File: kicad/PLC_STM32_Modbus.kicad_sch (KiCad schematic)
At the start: 0 parts

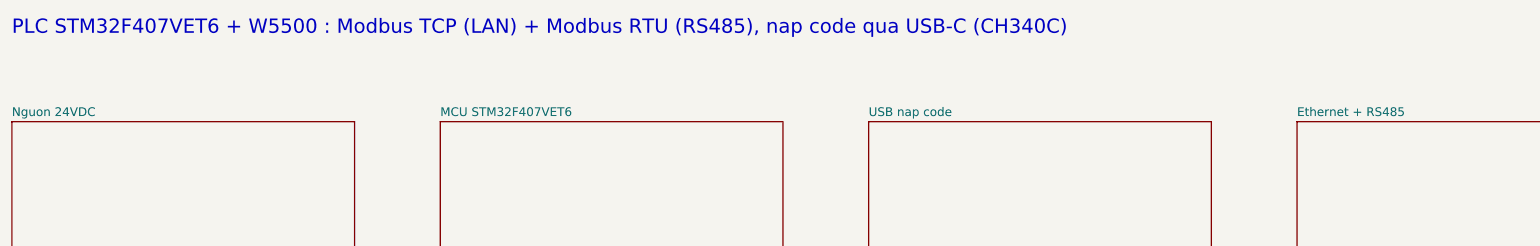
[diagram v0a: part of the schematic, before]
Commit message: - bỏ các mạch 0-10v, RS485 RTU
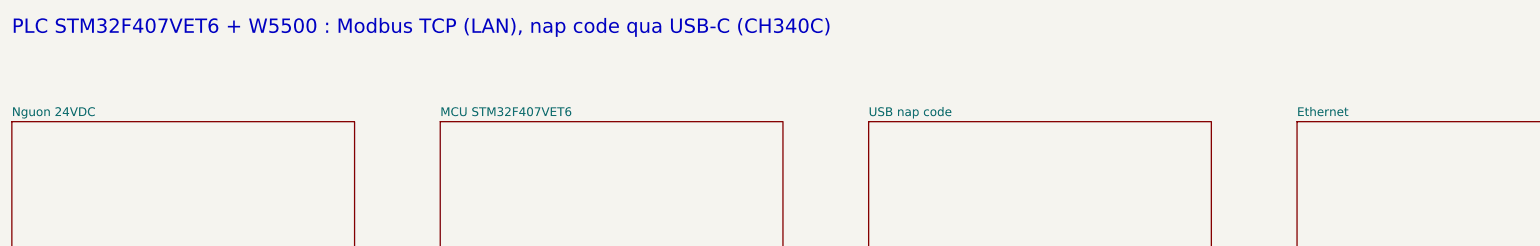
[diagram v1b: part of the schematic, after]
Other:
- removed sheet Ethernet + RS485
- added sheet Ethernet (comm.kicad_sch)
- note added: "PLC STM32F407VET6 + W5500 : Modbus TCP (LAN), nap code qua USB-C (CH340C)"
- note removed: "PLC STM32F407VET6 + W5500 : Modbus TCP (LAN) + Modbus RTU (RS485), nap code qua USB-C (CH340C)"
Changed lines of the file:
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@@
 (kicad_sch
-	(version 20250610)
+	(version 20260306)
 	(generator "eeschema")
 	(generator_version "10.0")
@@
 		(comment 1 "Sheet: Root")
 	)
-	(text "PLC STM32F407VET6 + W5500 : Modbus TCP (LAN) + Modbus RTU (RS485), nap code qua USB-C (CH340C)"
+	(text "PLC STM32F407VET6 + W5500 : Modbus TCP (LAN), nap code qua USB-C (CH340C)"
 		(exclude_from_sim no)
 		(at 30 25 0)
@@
 	)
 	(sheet
+		(at 180 40)
+		(size 60 25)
+		(exclude_from_sim no)
+		(in_bom yes)
+		(on_board yes)
+		(dnp no)
+		(stroke
+			(width 0.1524)
+			(type solid)
+		)
+		(fill
+			(color 0 0 0 0)
+		)
+		(property "Sheetname" "USB nap code"
+			(at 180 39.2 0)
+			(show_name no)
+			(do_not_autoplace no)
+			(effects
+				(font
+					(size 1.524 1.524)
+				)
+				(justify left bottom)
+			)
+		)
+		(property "Sheetfile" "usb.kicad_sch"
+			(at 180 65.6 0)
+			(show_name no)
+			(do_not_autoplace no)
+			(effects
+				(font
+					(size 1.27 1.27)
+				)
+				(justify left top)
+			)
+		)
+		(instances
+			(project "PLC_STM32_Modbus"
+				(path "/2be3e191-9af5-421c-aa34-3e3c37fa6c43"
+					(page "4")
+				)
+			)
+		)
+	)
+	(sheet
+		(at 105 40)
+		(size 60 25)
+		(exclude_from_sim no)
+		(in_bom yes)
+		(on_board yes)
+		(dnp no)
+		(stroke
+			(width 0.1524)
+			(type solid)
+		)
+		(fill
+			(color 0 0 0 0)
+		)
+		(property "Sheetname" "MCU STM32F407VET6"
+			(at 105 39.2 0)
+			(show_name no)
+			(do_not_autoplace no)
+			(effects
+				(font
+					(size 1.524 1.524)
+				)
+				(justify left bottom)
+			)
+		)
+		(property "Sheetfile" "mcu.kicad_sch"
+			(at 105 65.6 0)
+			(show_name no)
+			(do_not_autoplace no)
+			(effects
+				(font
+					(size 1.27 1.27)
+				)
+				(justify left top)
+			)
+		)
+		(instances
+			(project "PLC_STM32_Modbus"
+				(path "/2be3e191-9af5-421c-aa34-3e3c37fa6c43"
+					(page "3")
+				)
+			)
+		)
+	)
+	(sheet
+		(at 255 40)
+		(size 60 25)
+		(exclude_from_sim no)
+		(in_bom yes)
+		(on_board yes)
+		(dnp no)
+		(stroke
+			(width 0.1524)
+			(type solid)
+		)
+		(fill
+			(color 0 0 0 0)
+		)
+		(property "Sheetname" "Ethernet"
+			(at 255 39.2 0)
+			(show_name no)
+			(do_not_autoplace no)
+			(effects
+				(font
+					(size 1.524 1.524)
+				)
+				(justify left bottom)
+			)
+		)
+		(property "Sheetfile" "comm.kicad_sch"
+			(at 255 65.6 0)
+			(show_name no)
+			(do_not_autoplace no)
+			(effects
+				(font
+					(size 1.27 1.27)
+				)
+				(justify left top)
+			)
+		)
+		(instances
+			(project "PLC_STM32_Modbus"
+				(path "/2be3e191-9af5-421c-aa34-3e3c37fa6c43"
+					(page "5")
+				)
+			)
+		)
+	)
+	(sheet
 		(at 30 40)
 		(size 60 25)
@@
 		(property "Sheetname" "Nguon 24VDC"
 			(at 30 39.2 0)
+			(show_name no)
+			(do_not_autoplace no)
 			(effects
 				(font
@@
 		(property "Sheetfile" "power.kicad_sch"
 			(at 30 65.6 0)
-			(effects
-				(font
-					(size 1.27 1.27)
-				)
-				(justify left top)
-			)
-		)
-		(instances
-			(project "PLC_STM32_Modbus"
-				(path "/a82b7ef2-b1f1-4ce7-a1fb-fe132a934493"
+			(show_name no)
+			(do_not_autoplace no)
+			(effects
+				(font
+					(size 1.27 1.27)
+				)
+				(justify left top)
+			)
+		)
+		(instances
+			(project "PLC_STM32_Modbus"
+				(path "/2be3e191-9af5-421c-aa34-3e3c37fa6c43"
 					(page "2")
 				)
@@
 	)
 	(sheet
-		(at 105 40)
-		(size 60 25)
-		(exclude_from_sim no)
-		(in_bom yes)
-		(on_board yes)
-		(dnp no)
-		(stroke
-			(width 0.1524)
-			(type solid)
-		)
-		(fill
-			(color 0 0 0 0)
-		)
-		(property "Sheetname" "MCU STM32F407VET6"
-			(at 105 39.2 0)
-			(effects
-				(font
-					(size 1.524 1.524)
-				)
-				(justify left bottom)
-			)
-		)
-		(property "Sheetfile" "mcu.kicad_sch"
-			(at 105 65.6 0)
-			(effects
-				(font
-					(size 1.27 1.27)
-				)
-				(justify left top)
-			)
-		)
-		(instances
-			(project "PLC_STM32_Modbus"
-				(path "/a82b7ef2-b1f1-4ce7-a1fb-fe132a934493"
-					(page "3")
-				)
-			)
-		)
-	)
-	(sheet
-		(at 180 40)
-		(size 60 25)
-		(exclude_from_sim no)
-		(in_bom yes)
-		(on_board yes)
-		(dnp no)
-		(stroke
-			(width 0.1524)
-			(type solid)
-		)
-		(fill
-			(color 0 0 0 0)
-		)
-		(property "Sheetname" "USB nap code"
-			(at 180 39.2 0)
-			(effects
-				(font
-					(size 1.524 1.524)
-				)
-				(justify left bottom)
-			)
-		)
-		(property "Sheetfile" "usb.kicad_sch"
-			(at 180 65.6 0)
-			(effects
-				(font
-					(size 1.27 1.27)
-				)
-				(justify left top)
-			)
-		)
-		(instances
-			(project "PLC_STM32_Modbus"
-				(path "/a82b7ef2-b1f1-4ce7-a1fb-fe132a934493"
-					(page "4")
-				)
-			)
-		)
-	)
-	(sheet
-		(at 255 40)
-		(size 60 25)
-		(exclude_from_sim no)
-		(in_bom yes)
-		(on_board yes)
-		(dnp no)
-		(stroke
-			(width 0.1524)
-			(type solid)
-		)
-		(fill
-			(color 0 0 0 0)
-		)
-		(property "Sheetname" "Ethernet + RS485"
-			(at 255 39.2 0)
-			(effects
-				(font
-					(size 1.524 1.524)
-				)
-				(justify left bottom)
-			)
-		)
-		(property "Sheetfile" "comm.kicad_sch"
-			(at 255 65.6 0)
-			(effects
-				(font
-					(size 1.27 1.27)
-				)
-				(justify left top)
-			)
-		)
-		(instances
-			(project "PLC_STM32_Modbus"
-				(path "/a82b7ef2-b1f1-4ce7-a1fb-fe132a934493"
-					(page "5")
+		(at 105 85)
+		(size 60 25)
+		(exclude_from_sim no)
+		(in_bom yes)
+		(on_board yes)
+		(dnp no)
+		(stroke
+			(width 0.1524)
+			(type solid)
+		)
+		(fill
+			(color 0 0 0 0)
+		)
+		(property "Sheetname" "10 ngo vao analog"
+			(at 105 84.2 0)
+			(show_name no)
+			(do_not_autoplace no)
+			(effects
+				(font
+					(size 1.524 1.524)
+				)
+				(justify left bottom)
+			)
+		)
+		(property "Sheetfile" "analog.kicad_sch"
+			(at 105 110.6 0)
+			(show_name no)
+			(do_not_autoplace no)
+			(effects
+				(font
+					(size 1.27 1.27)
+				)
+				(justify left top)
+			)
+		)
+		(instances
+			(project "PLC_STM32_Modbus"
+				(path "/2be3e191-9af5-421c-aa34-3e3c37fa6c43"
+					(page "7")
 				)
 			)
@@
 		(property "Sheetname" "16 ngo ra transistor"
 			(at 30 84.2 0)
+			(show_name no)
+			(do_not_autoplace no)
 			(effects
 				(font
@@
 		(property "Sheetfile" "outputs.kicad_sch"
 			(at 30 110.6 0)
-			(effects
-				(font
-					(size 1.27 1.27)
-				)
-				(justify left top)
-			)
-		)
-		(instances
-			(project "PLC_STM32_Modbus"
-				(path "/a82b7ef2-b1f1-4ce7-a1fb-fe132a934493"
+			(show_name no)
+			(do_not_autoplace no)
+			(effects
+				(font
+					(size 1.27 1.27)
+				)
+				(justify left top)
+			)
+		)
+		(instances
+			(project "PLC_STM32_Modbus"
+				(path "/2be3e191-9af5-421c-aa34-3e3c37fa6c43"
 					(page "6")
 				)
 			)
-		)
-	)
-	(sheet
-		(at 105 85)
-		(size 60 25)
-		(exclude_from_sim no)
-		(in_bom yes)
-		(on_board yes)
-		(dnp no)
-		(stroke
-			(width 0.1524)
-			(type solid)
-		)
-		(fill
-			(color 0 0 0 0)
-		)
-		(property "Sheetname" "10 ngo vao analog"
-			(at 105 84.2 0)
-			(effects
-				(font
-					(size 1.524 1.524)
-				)
-				(justify left bottom)
-			)
-		)
-		(property "Sheetfile" "analog.kicad_sch"
-			(at 105 110.6 0)
-			(effects
-				(font
-					(size 1.27 1.27)
-				)
-				(justify left top)
-			)
-		)
-		(instances
-			(project "PLC_STM32_Modbus"
-				(path "/a82b7ef2-b1f1-4ce7-a1fb-fe132a934493"
-					(page "7")
-				)
-			)

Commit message: - bỏ các cầu chì thêm mô tả cho từng linh kiên
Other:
- note added: "TỔNG QUAN HỆ THỐNG – PLC STM32F407 + W5500 (Modbus TCP)"
- note added: "• Nguồn 24VDC → bảo vệ (PTC, chống ngược, TVS) + lọc nhiễu → buck 5V → LDO 3.3V; +3.3VA riêng cho ADC. • MCU STM32F407VET6 (168MHz): 16 ngõ ra DO1–DO16, 10 ngõ vào 4–20mA (ADC 12-bit, VREF 3.000V), SPI2 → W5500. • Ethernet W5500 + RJ45: Modbus TCP cổng 502, tối đa 8 kết nối. Coil 00001–00016 = DO1–DO16; Input Register 30001–30010 = AI1–AI10. • USB-C + CH340C: nạp chương trình qua bootloader UART 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"
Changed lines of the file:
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@@
+		)
+	)
+	(text "TỔNG QUAN HỆ THỐNG – PLC STM32F407 + W5500 (Modbus TCP)"
+		(exclude_from_sim no)
+		(at 30 125 0)
+		(effects
+			(font
+				(face "Arial")
+				(size 2 2)
+				(bold yes)
+				(color 0 0 132 1)
+			)
+			(justify left top)
+		)
+	)
+	(text "• Nguồn 24VDC → bảo vệ (PTC, chống ngược, TVS) + lọc nhiễu → buck 5V → LDO 3.3V; +3.3VA riêng cho ADC.\n• MCU STM32F407VET6 (168MHz): 16 ngõ ra DO1–DO16, 10 ngõ vào 4–20mA (ADC 12-bit, VREF 3.000V), SPI2 → W5500.\n• Ethernet W5500 + RJ45: Modbus TCP cổng 502, tối đa 8 kết nối. Coil 00001–00016 = DO1–DO16; Input Register 30001–30010 = AI1–AI10.\n• USB-C + CH340C: nạp chương trình qua bootloader UART (tự vào boot bằng DTR/RTS), cổng debug.\n• 16 ngõ ra: opto PC817 (cách ly 5kV) + MOSFET 60V/2.5A, kiểu sink, nguồn tải V+/COM riêng 12–30V.\n• 10 ngõ vào 4–20mA: TVS + shunt 120Ω + lọc RC; J703 cấp 24V (PTC 0.5A) nuôi cảm biến 2 dây.\n• Ghi chú chi tiết (tác dụng, cách tính giá trị) đặt ngay cạnh từng linh kiện ở các trang con."
+		(exclude_from_sim no)
+		(at 30 128.4 0)
+		(effects
+			(font
+				(face "Arial")
+				(size 1.6 1.6)
+				(color 0 0 132 1)
+			)
+			(justify left top)
+		)
+	)
+	(sheet
+		(at 105 40)
+		(size 60 25)
+		(exclude_from_sim no)
+		(in_bom yes)
+		(on_board yes)
+		(dnp no)
+		(stroke
+			(width 0.1524)
+			(type solid)
+		)
+		(fill
+			(color 0 0 0 0)
+		)
+		(property "Sheetname" "MCU STM32F407VET6"
+			(at 105 39.2 0)
+			(show_name no)
+			(do_not_autoplace no)
+			(effects
+				(font
+					(size 1.524 1.524)
+				)
+				(justify left bottom)
+			)
+		)
+		(property "Sheetfile" "mcu.kicad_sch"
+			(at 105 65.6 0)
+			(show_name no)
+			(do_not_autoplace no)
+			(effects
+				(font
+					(size 1.27 1.27)
+				)
+				(justify left top)
+			)
+		)
+		(instances
+			(project "PLC_STM32_Modbus"
+				(path "/2be3e191-9af5-421c-aa34-3e3c37fa6c43"
+					(page "4")
+				)
+			)
+		)
+	)
+	(sheet
+		(at 255 40)
+		(size 60 25)
+		(exclude_from_sim no)
+		(in_bom yes)
+		(on_board yes)
+		(dnp no)
+		(stroke
+			(width 0.1524)
+			(type solid)
+		)
+		(fill
+			(color 0 0 0 0)
+		)
+		(property "Sheetname" "Ethernet"
+			(at 255 39.2 0)
+			(show_name no)
+			(do_not_autoplace no)
+			(effects
+				(font
+					(size 1.524 1.524)
+				)
+				(justify left bottom)
+			)
+		)
+		(property "Sheetfile" "comm.kicad_sch"
+			(at 255 65.6 0)
+			(show_name no)
+			(do_not_autoplace no)
+			(effects
+				(font
+					(size 1.27 1.27)
+				)
+				(justify left top)
+			)
+		)
+		(instances
+			(project "PLC_STM32_Modbus"
+				(path "/2be3e191-9af5-421c-aa34-3e3c37fa6c43"
+					(page "7")
+				)
+			)
+		)
+	)
+	(sheet
+		(at 30 40)
+		(size 60 25)
+		(exclude_from_sim no)
+		(in_bom yes)
+		(on_board yes)
+		(dnp no)
+		(stroke
+			(width 0.1524)
+			(type solid)
+		)
+		(fill
+			(color 0 0 0 0)
+		)
+		(property "Sheetname" "Nguon 24VDC"
+			(at 30 39.2 0)
+			(show_name no)
+			(do_not_autoplace no)
+			(effects
+				(font
+					(size 1.524 1.524)
+				)
+				(justify left bottom)
+			)
+		)
+		(property "Sheetfile" "power.kicad_sch"
+			(at 30 65.6 0)
+			(show_name no)
+			(do_not_autoplace no)
+			(effects
+				(font
+					(size 1.27 1.27)
+				)
+				(justify left top)
+			)
+		)
+		(instances
+			(project "PLC_STM32_Modbus"
+				(path "/2be3e191-9af5-421c-aa34-3e3c37fa6c43"
+					(page "2")
+				)
+			)
+		)
+	)
+	(sheet
+		(at 30 85)
+		(size 60 25)
+		(exclude_from_sim no)
+		(in_bom yes)
+		(on_board yes)
+		(dnp no)
+		(stroke
+			(width 0.1524)
+			(type solid)
+		)
+		(fill
+			(color 0 0 0 0)
+		)
+		(property "Sheetname" "16 ngo ra transistor"
+			(at 30 84.2 0)
+			(show_name no)
+			(do_not_autoplace no)
+			(effects
+				(font
+					(size 1.524 1.524)
+				)
+				(justify left bottom)
+			)
+		)
+		(property "Sheetfile" "outputs.kicad_sch"
+			(at 30 110.6 0)
+			(show_name no)
+			(do_not_autoplace no)
+			(effects
+				(font
+					(size 1.27 1.27)
+				)
+				(justify left top)
+			)
+		)
+		(instances
+			(project "PLC_STM32_Modbus"
+				(path "/2be3e191-9af5-421c-aa34-3e3c37fa6c43"
+					(page "3")
+				)
+			)
 		)
 	)
@@
 			(project "PLC_STM32_Modbus"
 				(path "/2be3e191-9af5-421c-aa34-3e3c37fa6c43"
-					(page "4")
-				)
-			)
-		)
-	)
-	(sheet
-		(at 105 40)
-		(size 60 25)
-		(exclude_from_sim no)
-		(in_bom yes)
-		(on_board yes)
-		(dnp no)
-		(stroke
-			(width 0.1524)
-			(type solid)
-		)
-		(fill
-			(color 0 0 0 0)
-		)
-		(property "Sheetname" "MCU STM32F407VET6"
-			(at 105 39.2 0)
-			(show_name no)
-			(do_not_autoplace no)
-			(effects
-				(font
-					(size 1.524 1.524)
-				)
-				(justify left bottom)
-			)
-		)
-		(property "Sheetfile" "mcu.kicad_sch"
-			(at 105 65.6 0)
-			(show_name no)
-			(do_not_autoplace no)
-			(effects
-				(font
-					(size 1.27 1.27)
-				)
-				(justify left top)
-			)
-		)
-		(instances
-			(project "PLC_STM32_Modbus"
-				(path "/2be3e191-9af5-421c-aa34-3e3c37fa6c43"
-					(page "3")
-				)
-			)
-		)
-	)
-	(sheet
-		(at 255 40)
-		(size 60 25)
-		(exclude_from_sim no)
-		(in_bom yes)
-		(on_board yes)
-		(dnp no)
-		(stroke
-			(width 0.1524)
-			(type solid)
-		)
-		(fill
-			(color 0 0 0 0)
-		)
-		(property "Sheetname" "Ethernet"
-			(at 255 39.2 0)
-			(show_name no)
-			(do_not_autoplace no)
-			(effects
-				(font
-					(size 1.524 1.524)
-				)
-				(justify left bottom)
-			)
-		)
-		(property "Sheetfile" "comm.kicad_sch"
-			(at 255 65.6 0)
-			(show_name no)
-			(do_not_autoplace no)
-			(effects
-				(font
-					(size 1.27 1.27)
-				)
-				(justify left top)
-			)
-		)
-		(instances
-			(project "PLC_STM32_Modbus"
-				(path "/2be3e191-9af5-421c-aa34-3e3c37fa6c43"
-					(page "5")
-				)
-			)
-		)
-	)
-	(sheet
-		(at 30 40)
-		(size 60 25)
-		(exclude_from_sim no)
-		(in_bom yes)
-		(on_board yes)
-		(dnp no)
-		(stroke
-			(width 0.1524)
-			(type solid)
-		)
-		(fill
-			(color 0 0 0 0)
-		)
-		(property "Sheetname" "Nguon 24VDC"
-			(at 30 39.2 0)
-			(show_name no)
-			(do_not_autoplace no)
-			(effects
-				(font
-					(size 1.524 1.524)
-				)
-				(justify left bottom)
-			)
-		)
-		(property "Sheetfile" "power.kicad_sch"
-			(at 30 65.6 0)
-			(show_name no)
-			(do_not_autoplace no)
-			(effects
-				(font
-					(size 1.27 1.27)
-				)
-				(justify left top)
-			)
-		)
-		(instances
-			(project "PLC_STM32_Modbus"
-				(path "/2be3e191-9af5-421c-aa34-3e3c37fa6c43"
-					(page "2")
+					(page "6")
 				)
 			)
@@
 			(project "PLC_STM32_Modbus"
 				(path "/2be3e191-9af5-421c-aa34-3e3c37fa6c43"
-					(page "7")
-				)
-			)
-		)
-	)
-	(sheet
-		(at 30 85)
-		(size 60 25)
-		(exclude_from_sim no)
-		(in_bom yes)
-		(on_board yes)
-		(dnp no)
-		(stroke
-			(width 0.1524)
-			(type solid)
-		)
-		(fill
-			(color 0 0 0 0)
-		)
-		(property "Sheetname" "16 ngo ra transistor"
-			(at 30 84.2 0)
-			(show_name no)
-			(do_not_autoplace no)
-			(effects
-				(font
-					(size 1.524 1.524)
-				)
-				(justify left bottom)
-			)
-		)
-		(property "Sheetfile" "outputs.kicad_sch"
-			(at 30 110.6 0)
-			(show_name no)
-			(do_not_autoplace no)
-			(effects
-				(font
-					(size 1.27 1.27)
-				)
-				(justify left top)
-			)
-		)
-		(instances
-			(project "PLC_STM32_Modbus"
-				(path "/2be3e191-9af5-421c-aa34-3e3c37fa6c43"
-					(page "6")
-				)
-			)
+					(page "5")
+				)
+			)
